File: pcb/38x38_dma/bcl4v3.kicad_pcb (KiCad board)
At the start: 2 copper layers, 38 x 38 mm, 30 parts, among them J1 Conn_01x04, J10 Conn_01x04, J2 Conn_01x04, J3 Conn_01x04, J4 Conn_01x04, J5 Conn_01x04, J6 Conn_01x04, J7 Conn_01x04, J8 Conn_01x04, J9 10118194-0001LF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

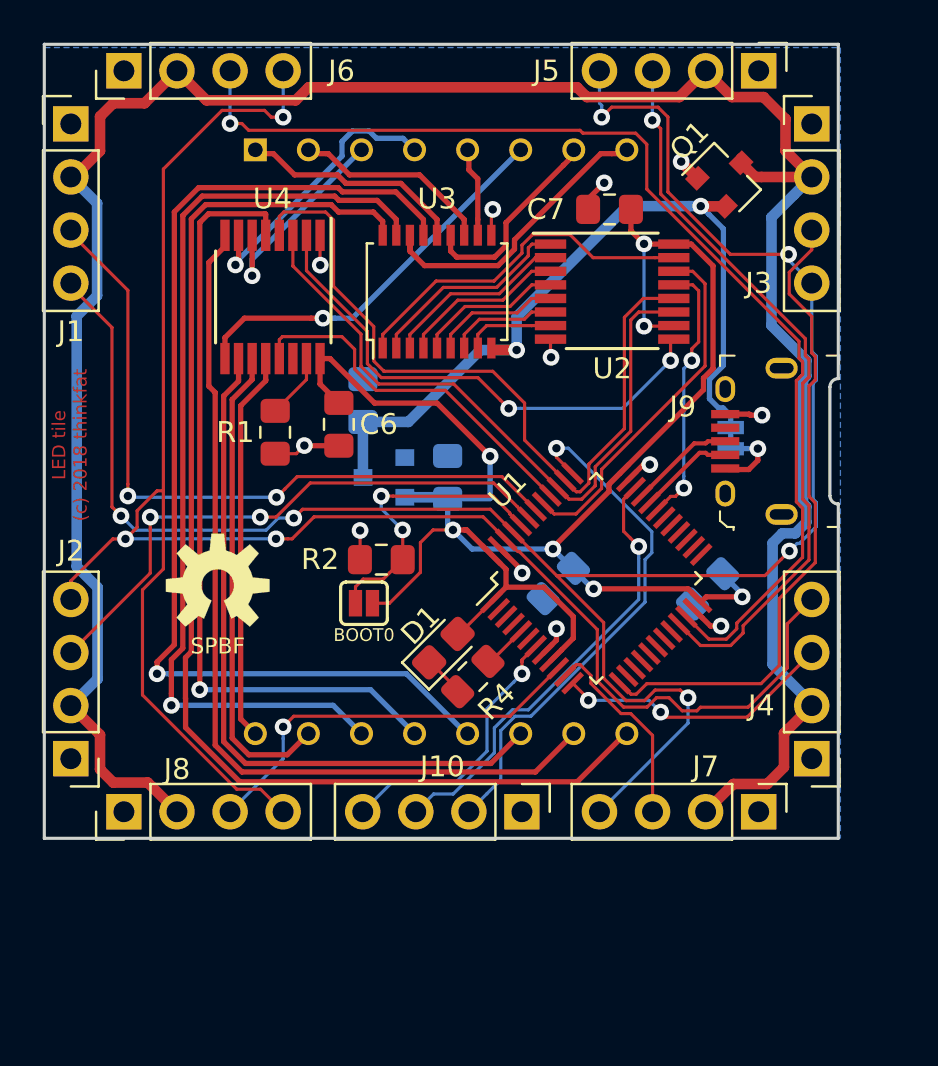
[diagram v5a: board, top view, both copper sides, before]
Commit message: Add test points, small routing changes
- add test points for SPI bus
- add net classes for VCC and LED networks
- small routing changes
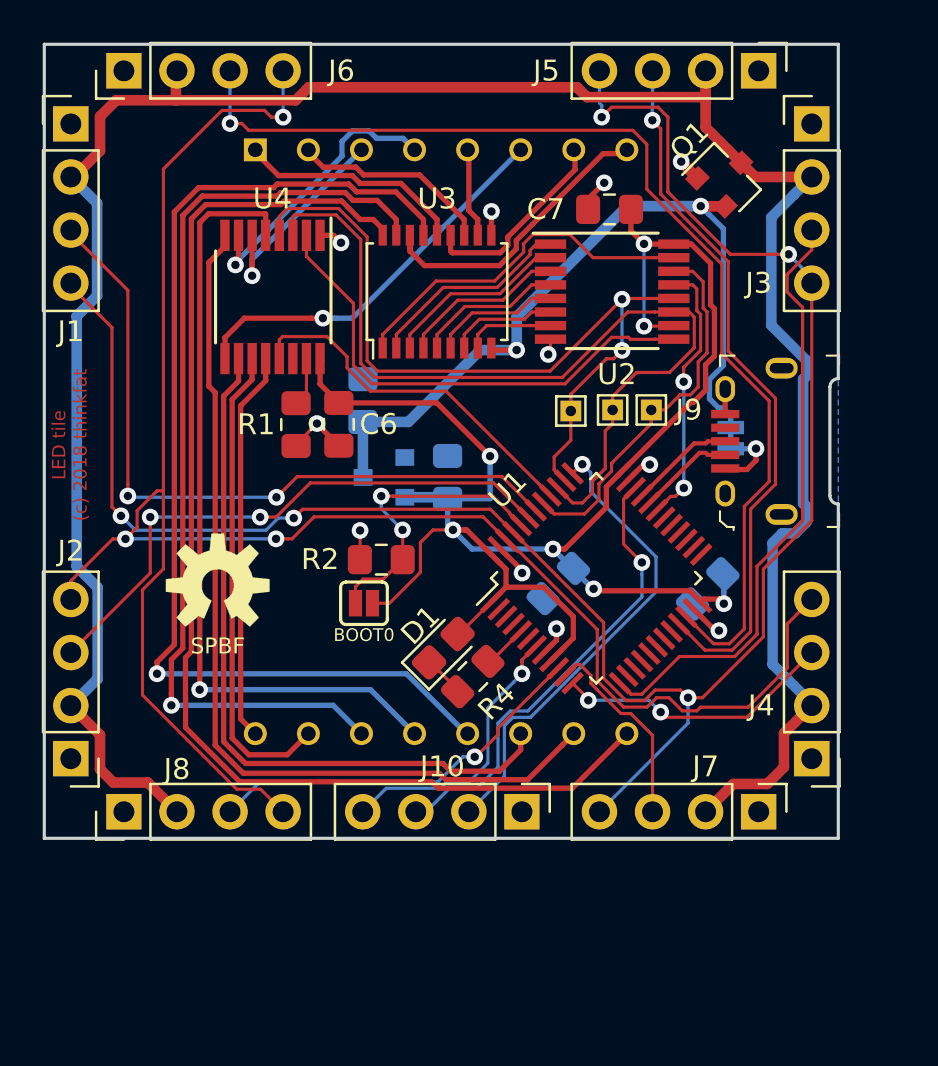
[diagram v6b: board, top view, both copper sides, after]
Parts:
- added TP1: TestPoint, TestPoint:TestPoint_THTPad_1.0x1.0mm_Drill0.5mm, F.Cu at (141.2, 81.5)
- added TP2: TestPoint, TestPoint:TestPoint_THTPad_1.0x1.0mm_Drill0.5mm, F.Cu at (139.2, 81.5)
- added TP3: TestPoint, TestPoint:TestPoint_THTPad_1.0x1.0mm_Drill0.5mm, F.Cu at (143.1, 81.5)
- LOGO1: footprint OSHW-LOGO-M -> Aesthetics:OSHW-LOGO-M
- moved R1 1.07 mm to (126.0, 82.2)
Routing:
- net /CAT_CLK: track 32.6 -> 41.7 mm
- net VCC: track 119.0 -> 115.8 mm
- net /I2C_SDA: track 96.3 -> 93.7 mm, vias 6 -> 5
- net /SWCLK: track 25.2 -> 22.9 mm
- net +3V3: track 85.1 -> 82.9 mm
- net /UART2_RX: track 31.2 -> 29.0 mm
- net /CAT_STROBE: track 36.7 -> 38.5 mm, vias 0 -> 2
- net /UART3_TX: track 35.3 -> 34.1 mm
- net /UART3_RX: track 53.6 -> 52.4 mm
- net GND: track 18.7 -> 17.5 mm, vias 12 -> 11
- net /CAT_DATA: track 17.1 -> 18.1 mm
- net Net-(U2-Pad9): track 24.8 -> 23.8 mm, vias 2 -> 0
- net Net-(R1-Pad1): track 3.12 -> 2.34 mm
- net /COL_6: track 33.9 -> 34.6 mm
- net /UART4_TX: track 19.4 -> 18.7 mm
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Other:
- net class VCC added: clearance 0.1524, trace_width 0.508, via_dia 0.8, via_drill 0.4
- net class VCC_LOW added: clearance 0.1524, trace_width 0.254, via_dia 0.8, via_drill 0.4

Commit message: small pcb fixes
move USB_VBUS via out from under the USB receptacle (ouch)
it just makes handsoldering difficult because the shield of
the receptacle sucks up superfluous tin and then shorts
USB_VBUS to ground
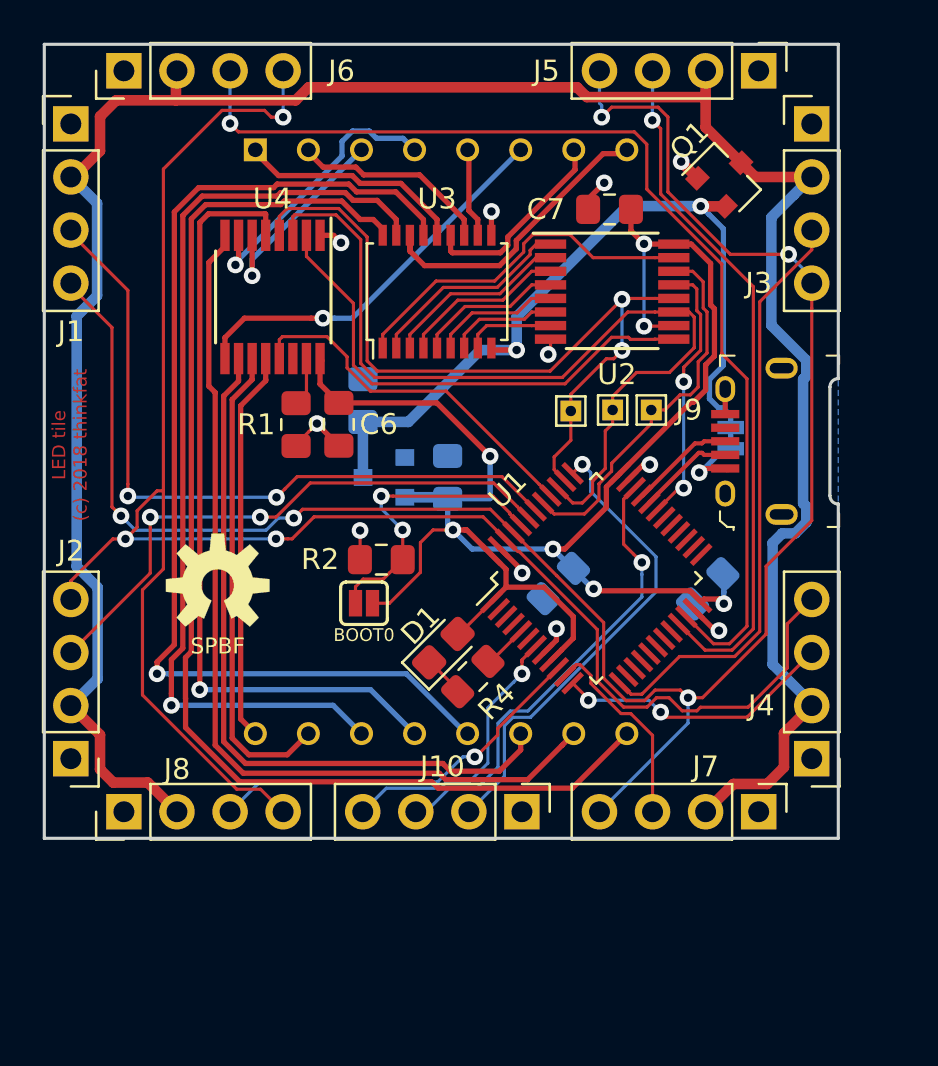
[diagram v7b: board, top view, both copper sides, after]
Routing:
- net /UART3_TX: track 34.1 -> 33.2 mm
- net /UART3_RX: track 52.4 -> 51.6 mm
- net /UART2_RX: track 29.0 -> 28.4 mm

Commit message: Sync GPIO corrections, add tactile switch for BOOT0 signal
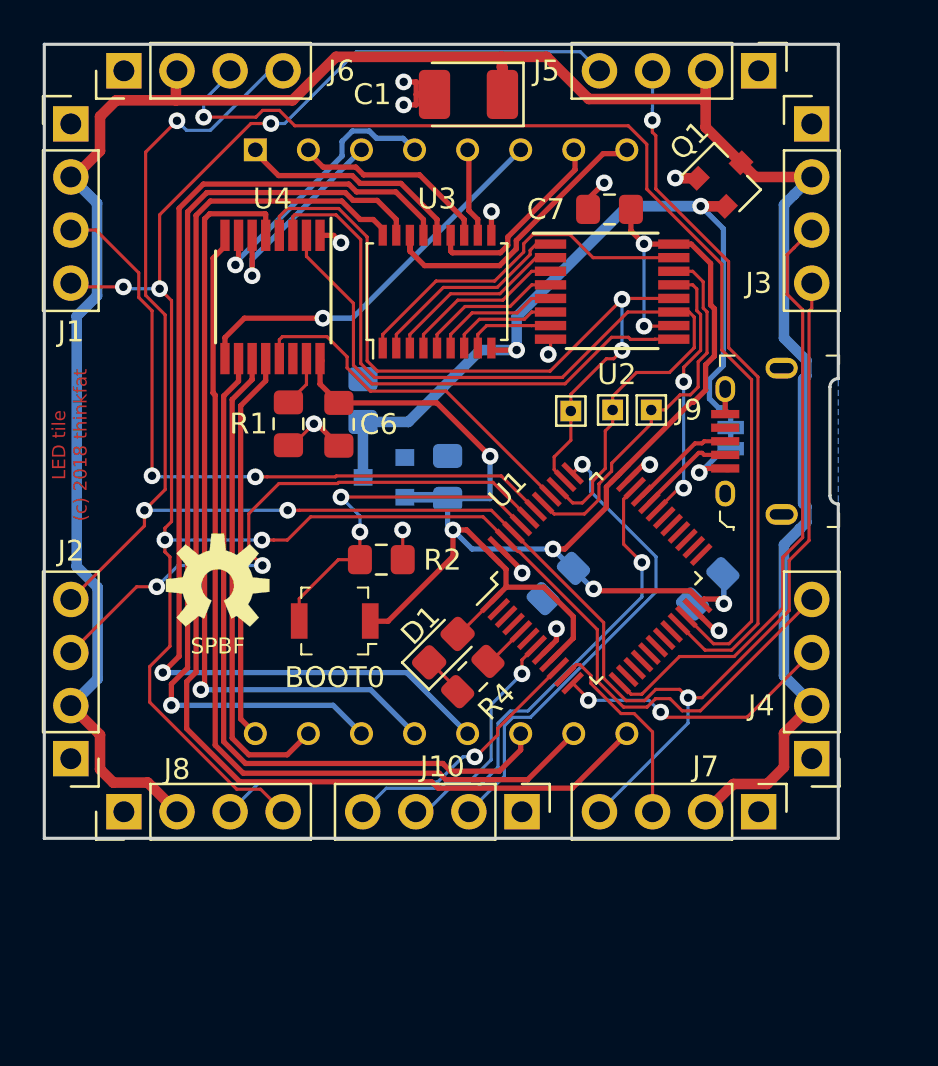
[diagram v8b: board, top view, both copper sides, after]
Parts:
- added C1: 22µF, Capacitor_Tantalum_SMD:CP_EIA-3528-15_AVX-H_Pad1.50x2.35mm_HandSolder, F.Cu at (134.3, 66.4)
- BOOT0: value Jumper_2_Open -> B3U-1000P; footprint Jumpers:SMT-JUMPER_2_NO_SILK -> digikey-footprints:Switch_Tactile_SMD_B3U-1000P
- moved BOOT0 1.64 mm to (127.9, 91.6)
- moved R1 0.37 mm to (125.7, 82.2)
- turned R2 to 0 degrees
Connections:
- J1 pad 4: /I2C_SDA -> /SYN_TX
- J2 pad 4: /I2C_SCL -> /SYN_RX
- J3 pad 4: /I2C_SDA -> /SYN_RX
- J4 pad 4: /I2C_SCL -> /SYN_TX
- J5 pad 4: /I2C_SDA -> /SYN_TX
- J6 pad 4: /I2C_SCL -> /SYN_RX
- J7 pad 4: /I2C_SDA -> /SYN_RX
- J8 pad 4: /I2C_SCL -> /SYN_TX
- U1 pad 45: /I2C_SDA -> /SYN_RX
- U1 pad 46: /I2C_SCL -> /SYN_TX
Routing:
- net /SYN_TX: track 0.00 -> 101.0 mm, vias 0 -> 5
- net /SYN_RX: track 0.00 -> 94.1 mm, vias 0 -> 4
- net /I2C_SDA: track 93.7 -> 0.00 mm, vias 5 -> 0
- net /I2C_SCL: track 93.6 -> 0.00 mm, vias 3 -> 0
- net GND: track 17.5 -> 20.8 mm, vias 11 -> 13
- net /BOOT0: track 14.3 -> 17.3 mm
- net /UART3_RX: track 51.6 -> 53.6 mm
- net VCC: track 115.8 -> 117.6 mm
- net /UART1_TX: track 34.3 -> 33.2 mm
- net /UART1_RX: track 27.5 -> 28.3 mm
- net /UART2_RX: track 28.4 -> 29.0 mm
